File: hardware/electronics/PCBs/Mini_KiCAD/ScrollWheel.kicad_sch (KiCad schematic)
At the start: 7 parts

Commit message: Initial commit of the modified Ploopy Mini PCB with RP2040, PMW3360 and mid-mounted USB-C
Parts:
- SCW.D.11, SCW.D.12: footprint IR12-21C/TR8 -> LEDs:XZTHI56W-1
- SCW.Qt.1, SCW.Qt.2: footprint PT26-51B/TR8 -> OptoElectronics.PcbLib:PT26-51B_TR8
- SCW.R.1, SCW.R.2: footprint 0805 -> Chip_Passives.PcbLib:0805
- SCW.R.4: renamed from SCW.r.4; footprint 0805 -> Chip_Passives.PcbLib:0805
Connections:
- net SCW.D11: now reaches SCW.D.11.C, SCW.D.12.A
- net V_USB renamed 3V3
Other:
- note removed: "${CURRENTTIME}"
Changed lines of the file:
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@@
 		)
 	)
-	(text "${CURRENTTIME}"
-		(exclude_from_sim no)
-		(at 194.31 210.82 0)
+	(text "${##}"
+		(exclude_from_sim no)
+		(at 233.68 210.82 0)
 		(effects
 			(font
@@
 		)
 	)
-	(text "${##}"
-		(exclude_from_sim no)
-		(at 233.68 210.82 0)
+	(text "of"
+		(exclude_from_sim no)
+		(at 230.632 210.82 0)
 		(effects
 			(font
@@
 		)
 	)
-	(text "of"
-		(exclude_from_sim no)
-		(at 230.632 210.82 0)
+	(text "${CURRENT_DATE}"
+		(exclude_from_sim no)
+		(at 175.26 210.82 0)
 		(effects
 			(font
@@
 		)
 	)
-	(text "${CURRENT_DATE}"
-		(exclude_from_sim no)
-		(at 175.26 210.82 0)
+	(text "http://ohwr.org/cernohl"
+		(exclude_from_sim no)
+		(at 124.46 208.28 0)
+		(effects
+			(font
+				(size 1.397 1.397)
+			)
+			(justify left bottom)
+		)
+	)
+	(text "Title:"
+		(exclude_from_sim no)
+		(at 168.91 201.93 0)
 		(effects
 			(font
@@
 		)
 	)
-	(text "http://ohwr.org/cernohl"
-		(exclude_from_sim no)
-		(at 124.46 208.28 0)
-		(effects
-			(font
-				(size 1.397 1.397)
-			)
-			(justify left bottom)
-		)
-	)
-	(text "Title:"
-		(exclude_from_sim no)
-		(at 168.91 201.93 0)
+	(text "Ploopy Corporation"
+		(exclude_from_sim no)
+		(at 241.3 202.438 0)
+		(effects
+			(font
+				(size 1.651 1.651)
+			)
+			(justify left bottom)
+		)
+	)
+	(text "${PROJECTNAME}"
+		(exclude_from_sim no)
+		(at 174.752 207.264 0)
+		(effects
+			(font
+				(size 1.651 1.651)
+			)
+			(justify left bottom)
+		)
+	)
+	(text "137-1140 Burnhamthorpe Road W"
+		(exclude_from_sim no)
+		(at 241.3 204.978 0)
 		(effects
 			(font
@@
 		)
 	)
-	(text "Ploopy Corporation"
-		(exclude_from_sim no)
-		(at 241.3 202.438 0)
-		(effects
-			(font
-				(size 1.651 1.651)
-			)
-			(justify left bottom)
-		)
-	)
-	(text "${PROJECTNAME}"
-		(exclude_from_sim no)
-		(at 174.752 207.264 0)
-		(effects
-			(font
-				(size 1.651 1.651)
-			)
-			(justify left bottom)
-		)
-	)
-	(text "137-1140 Burnhamthorpe Road W"
-		(exclude_from_sim no)
-		(at 241.3 204.978 0)
-		(effects
-			(font
-				(size 1.143 1.143)
-			)
-			(justify left bottom)
-		)
-	)
-	(label "V_USB"
+	(label "3V3"
 		(at 91.44 60.96 0)
 		(fields_autoplaced yes)
@@
 		)
 	)
-	(label "V_USB"
+	(label "SCW.D11"
+		(at 101.6 110.49 0)
+		(fields_autoplaced yes)
+		(effects
+			(font
+				(size 1.27 1.27)
+			)
+			(justify left bottom)
+		)
+	)
+	(label "3V3"
+		(at 139.7 60.96 0)
+		(fields_autoplaced yes)
+		(effects
+			(font
+				(size 1.27 1.27)
+			)
+			(justify left bottom)
+		)
+	)
+	(label "3V3"
 		(at 142.24 114.3 0)
-		(fields_autoplaced yes)
-		(effects
-			(font
-				(size 1.27 1.27)
-			)
-			(justify left bottom)
-		)
-	)
-	(label "V_USB"
-		(at 139.7 60.96 0)
 		(fields_autoplaced yes)
 		(effects
@@
 		)
 	)
+	(hierarchical_label "3V3"
+		(shape input)
+		(at 142.24 114.3 180)
+		(fields_autoplaced yes)
+		(effects
+			(font
+				(size 1.27 1.27)
+			)
+			(justify right)
+		)
+	)
 	(hierarchical_label "ScrollWheelOpto1"
 		(shape output)
@@
 		)
 	)
-	(hierarchical_label "V_USB"
+	(hierarchical_label "3V3"
+		(shape input)
+		(at 139.7 60.96 180)
+		(fields_autoplaced yes)
+		(effects
+			(font
+				(size 1.27 1.27)
+			)
+			(justify right)
+		)
+	)
+	(hierarchical_label "3V3"
 		(shape input)
 		(at 91.44 60.96 180)
@@
 		(on_board yes)
 		(dnp no)
-		(property "Reference" "SCW.r.4"
+		(property "Reference" "SCW.R.4"
 			(at 153.162 136.906 0)
 			(effects
@@
 			)
 		)
-		(property "Footprint" "0805"
+		(property "Footprint" "Chip_Passives.PcbLib:0805"
 			(at 149.86 139.7 0)
 			(effects
@@
 			(project "Mini"
 				(path "/4010ea29-f248-4f19-83ee-6b19cd4442a4/10daec88-f6fe-4771-a75f-0b8234f02ca1"
-					(reference "SCW.r.4")
+					(reference "SCW.R.4")
 					(unit 1)
 				)
@@
 			)
 		)
-		(property "Footprint" "PT26-51B/TR8"
+		(property "Footprint" "OptoElectronics.PcbLib:PT26-51B_TR8"
 			(at 152.4 124.46 0)
 			(effects
@@
 			)
 		)
-		(property "Footprint" "IR12-21C/TR8"
+		(property "Footprint" "LEDs:XZTHI56W-1"
 			(at 101.6 78.74 0)
 			(effects
@@
 			)
 		)
-		(property "Footprint" "0805"
+		(property "Footprint" "Chip_Passives.PcbLib:0805"
 			(at 149.86 86.36 0)
 			(effects
@@
 			)
 		)
-		(property "Footprint" "0805"
+		(property "Footprint" "Chip_Passives.PcbLib:0805"
 			(at 99.06 71.12 0)
 			(effects
@@
 			)
 		)
-		(property "Footprint" "PT26-51B/TR8"
+		(property "Footprint" "OptoElectronics.PcbLib:PT26-51B_TR8"
 			(at 152.4 71.12 0)
 			(effects
@@
 			)
 		)
-		(property "Footprint" "IR12-21C/TR8"
+		(property "Footprint" "LEDs:XZTHI56W-1"
 			(at 101.6 132.08 0)
 			(effects

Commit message: Rerouted the SPI devices and general cleanup, relocated all associated footprint library inside the project folder
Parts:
- SCW.Qt.1, SCW.Qt.2: footprint OptoElectronics.PcbLib:PT26-51B_TR8 -> OptoElectronics:PT26-51B_TR8
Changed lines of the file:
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@@
 			)
 		)
-		(property "Footprint" "OptoElectronics.PcbLib:PT26-51B_TR8"
+		(property "Footprint" "OptoElectronics:PT26-51B_TR8"
 			(at 152.4 124.46 0)
 			(effects
@@
 			)
 		)
-		(property "Footprint" "OptoElectronics.PcbLib:PT26-51B_TR8"
+		(property "Footprint" "OptoElectronics:PT26-51B_TR8"
 			(at 152.4 71.12 0)
 			(effects

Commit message: Resolved most DRC errors and re-annotated the schematic to be friendly to BOM generation.
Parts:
- SCW.R.1: value 0805 -> 100R 1%
- SCW.R.2, SCW.R.4: value 0805 -> 1k 1%
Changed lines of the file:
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@@
 			)
 		)
-		(property "Value" "0805"
+		(property "Value" "1k 1%"
 			(at 153.162 139.446 0)
 			(effects
@@
 				)
 				(justify left bottom)
+				(hide yes)
 			)
 		)
@@
 			)
 		)
-		(property "Value" "0805"
+		(property "Value" "1k 1%"
 			(at 153.162 86.106 0)
 			(effects
@@
 				)
 				(justify left bottom)
+				(hide yes)
 			)
 		)
@@
 			)
 		)
-		(property "Value" "0805"
+		(property "Value" "100R 1%"
 			(at 102.362 70.866 0)
 			(effects
@@
 				)
 				(justify left bottom)
-			)
-		)
+				(hide yes)
+			)
+		)

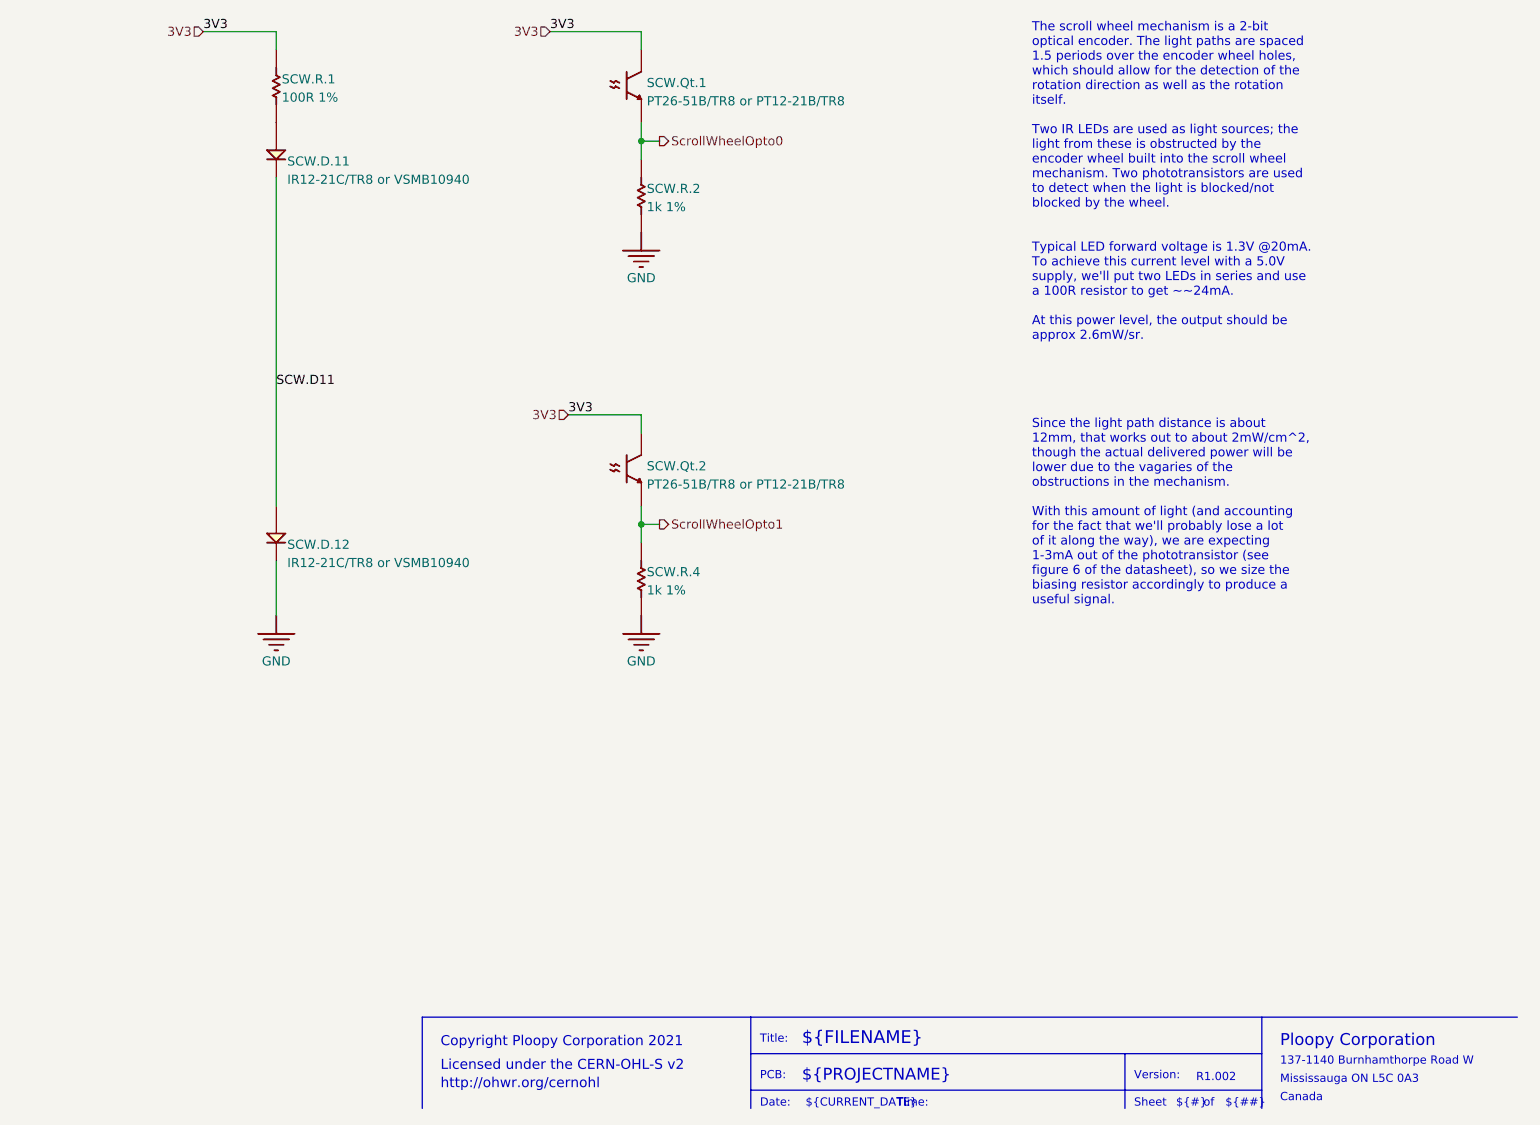
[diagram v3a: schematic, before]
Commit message: Rev1.002 Replaced all symbols in the schematic with built-in symbols where applicable. Reoriented the sensor to solve interference and tracking issues. Replaced the mid-mount USB port with regular port.
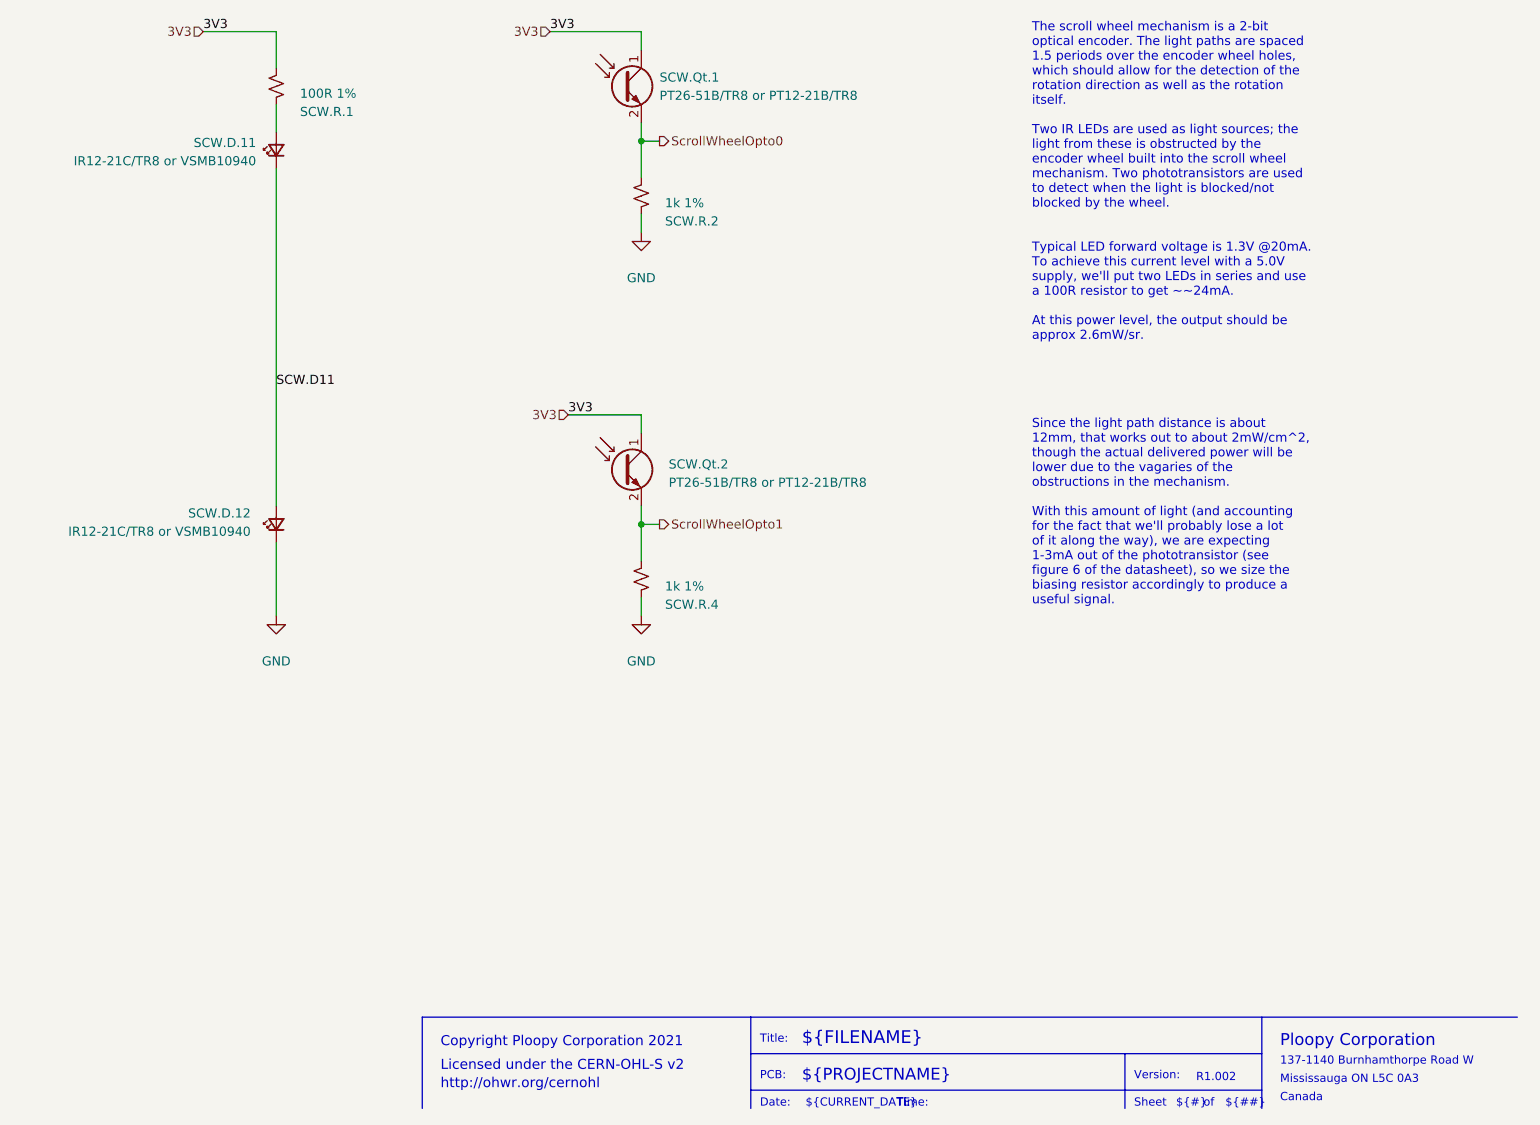
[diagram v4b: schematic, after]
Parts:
- removed SCW.Qt.1, SCW.Qt.2: PT26-51B/TR8 or PT12-21B/TR8, OptoElectronics:PT26-51B_TR8, symbol Mini-altium-import:SCW_1_PT26-51B/TR8
- added SCW.Qt.1, SCW.Qt.2: PT26-51B/TR8 or PT12-21B/TR8, OptoElectronics:PT26-51B_TR8, symbol Device:Q_Photo_NPN
- SCW.D.11, SCW.D.12: symbol Mini-altium-import:SCW_1_IR12-21C/TR8 -> Device:LED_Small
- SCW.R.1: symbol Mini-altium-import:SCW_1_Res 100R 1% 0805 -> Device:R_Small_US
- SCW.R.2, SCW.R.4: symbol Mini-altium-import:SCW_1_Res 1k 1% 0805 -> Device:R_Small_US
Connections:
- net 3V3: now also SCW.Qt.1.1 (C), SCW.Qt.2.1 (C)
- net GND: now also SCW.D.12.1 (K); no longer SCW.D.12.C
- net SCW.D11: now also SCW.D.11.1 (K), SCW.D.12.2 (A); no longer SCW.D.11.C, SCW.D.12.A
- net ScrollWheelOpto0: now also SCW.Qt.1.2 (E)
- net ScrollWheelOpto1: now also SCW.Qt.2.2 (E)
- net at SCW.R.1.1: now also SCW.D.11.2 (A); no longer SCW.D.11.A
